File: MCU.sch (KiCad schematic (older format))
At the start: 14 parts, among them U1 STM32F405RGTx, U2 ADR4533BRZ, Y1 Crystal_GND24

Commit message: Finished first version of schematic
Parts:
- C20: renamed from C3; footprint (none) -> Capacitor_SMD:C_0603_1608Metric
- C21: renamed from C4; footprint (none) -> Capacitor_SMD:C_0603_1608Metric
- C22: renamed from C5; footprint (none) -> Capacitor_SMD:C_0603_1608Metric
- C23: renamed from C6; footprint (none) -> Capacitor_SMD:C_0603_1608Metric
- C24: renamed from C7; footprint (none) -> Capacitor_SMD:C_0603_1608Metric
- C25: renamed from C8; footprint (none) -> Capacitor_SMD:C_0603_1608Metric
- C26: renamed from C9; footprint (none) -> Capacitor_SMD:C_0603_1608Metric
- C27: renamed from C10; footprint (none) -> Capacitor_SMD:C_0603_1608Metric
- C28: renamed from C11; footprint (none) -> Capacitor_SMD:C_0603_1608Metric
- C29: renamed from C12; footprint (none) -> Capacitor_SMD:C_0603_1608Metric
- C30: renamed from C13; footprint (none) -> Capacitor_SMD:C_0603_1608Metric
- Y1: footprint (none) -> Crystal:Crystal_SMD_Abracon_ABM3C-4Pin_5.0x3.2mm
- renumbered U1 to U7, U2 to U8
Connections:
- net labels added: PB7_OUT_EN, PC2_ADC123_12, PC3_ADC123_13
- net labels removed: GNDA, PB7_VSEL_6, PB8_VSEL_7, PB9_VSEL_8
- no-connect marks 0 -> 18
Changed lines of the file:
@@
 $Descr A4 11693 8268
 encoding utf-8
-Sheet 2 4
-Title ""
-Date ""
-Rev ""
-Comp ""
+Sheet 4 5
+Title "Z Sim"
+Date "2019-10-22"
+Rev "0.1"
+Comp "ELp"
 Comment1 ""
 Comment2 ""
@@
 $EndDescr
 $Comp
-L MCU_ST_STM32F4:STM32F405RGTx U1
+L MCU_ST_STM32F4:STM32F405RGTx U7
 U 1 1 5DADBC00
 P 5750 3600
-F 0 "U1" H 5150 1811 50  0000 C CNN
+F 0 "U7" H 5150 1811 50  0000 C CNN
 F 1 "STM32F405RGTx" H 5150 1720 50  0000 C CNN
 F 2 "Package_QFP:LQFP-64_10x10mm_P0.5mm" H 5150 1900 50  0001 R CNN
@@
 	5050 3300 4450 3300
 $Comp
-L power:GND #PWR0111
+L power:GND #PWR031
 U 1 1 5DAEB085
 P 3050 3250
-F 0 "#PWR0111" H 3050 3000 50  0001 C CNN
+F 0 "#PWR031" H 3050 3000 50  0001 C CNN
 F 1 "GND" H 3055 3077 50  0000 C CNN
 F 2 "" H 3050 3250 50  0001 C CNN
@@
 $EndComp
 $Comp
-L Device:C_Small C8
+L Device:C_Small C25
 U 1 1 5DAEB516
 P 4750 2350
-F 0 "C8" V 4700 2450 50  0000 C CNN
+F 0 "C25" V 4700 2450 50  0000 C CNN
 F 1 "2.2u" V 4800 2500 50  0000 C CNN
-F 2 "" H 4750 2350 50  0001 C CNN
+F 2 "Capacitor_SMD:C_0603_1608Metric" H 4750 2350 50  0001 C CNN
 F 3 "~" H 4750 2350 50  0001 C CNN
 	1    4750 2350
@@
 $EndComp
 $Comp
-L Device:C_Small C9
+L Device:C_Small C26
 U 1 1 5DAECD7A
 P 4750 2550
-F 0 "C9" V 4700 2650 50  0000 C CNN
+F 0 "C26" V 4700 2650 50  0000 C CNN
 F 1 "2.2u" V 4800 2700 50  0000 C CNN
-F 2 "" H 4750 2550 50  0001 C CNN
+F 2 "Capacitor_SMD:C_0603_1608Metric" H 4750 2550 50  0001 C CNN
 F 3 "~" H 4750 2550 50  0001 C CNN
 	1    4750 2550
@@
 	3900 2700 3900 2950
 $Comp
-L Device:C_Small C3
+L Device:C_Small C20
 U 1 1 5DAE6AD0
 P 3350 2850
-F 0 "C3" H 3442 2896 50  0000 L CNN
+F 0 "C20" H 3442 2896 50  0000 L CNN
 F 1 "22p" H 3442 2805 50  0000 L CNN
-F 2 "" H 3350 2850 50  0001 C CNN
+F 2 "Capacitor_SMD:C_0603_1608Metric" H 3350 2850 50  0001 C CNN
 F 3 "~" H 3350 2850 50  0001 C CNN
 	1    3350 2850
@@
 $EndComp
 $Comp
-L Device:C_Small C4
+L Device:C_Small C21
 U 1 1 5DAE66B4
 P 3350 3450
-F 0 "C4" H 3442 3496 50  0000 L CNN
+F 0 "C21" H 3442 3496 50  0000 L CNN
 F 1 "22p" H 3442 3405 50  0000 L CNN
-F 2 "" H 3350 3450 50  0001 C CNN
+F 2 "Capacitor_SMD:C_0603_1608Metric" H 3350 3450 50  0001 C CNN
 F 3 "~" H 3350 3450 50  0001 C CNN
 	1    3350 3450
@@
 F 0 "Y1" V 3854 3494 50  0000 L CNN
 F 1 "Crystal_GND24" V 3550 3300 50  0000 L CNN
-F 2 "" H 3900 3250 50  0001 C CNN
+F 2 "Crystal:Crystal_SMD_Abracon_ABM3C-4Pin_5.0x3.2mm" H 3900 3250 50  0001 C CNN
 F 3 "~" H 3900 3250 50  0001 C CNN
 	1    3900 3250
@@
 	3350 3250 3700 3250
 $Comp
-L power:GND #PWR0112
+L power:GND #PWR034
 U 1 1 5DAF9103
 P 4600 2650
-F 0 "#PWR0112" H 4600 2400 50  0001 C CNN
+F 0 "#PWR034" H 4600 2400 50  0001 C CNN
 F 1 "GND" H 4750 2550 50  0000 C CNN
 F 2 "" H 4600 2650 50  0001 C CNN
@@
 	4450 3200 5050 3200
 $Comp
-L Device:C_Small C11
+L Device:C_Small C28
 U 1 1 5DB007EA
 P 5000 1400
-F 0 "C11" V 4950 1600 50  0000 C CNN
+F 0 "C28" V 4950 1600 50  0000 C CNN
 F 1 "2.2u" V 5050 1550 50  0000 C CNN
-F 2 "" H 5000 1400 50  0001 C CNN
+F 2 "Capacitor_SMD:C_0603_1608Metric" H 5000 1400 50  0001 C CNN
 F 3 "~" H 5000 1400 50  0001 C CNN
 	1    5000 1400
@@
 $EndComp
 $Comp
-L Device:C_Small C10
+L Device:C_Small C27
 U 1 1 5DB01DE1
 P 4800 1400
-F 0 "C10" V 4750 1600 50  0000 C CNN
+F 0 "C27" V 4750 1600 50  0000 C CNN
 F 1 "2.2u" V 4850 1550 50  0000 C CNN
-F 2 "" H 4800 1400 50  0001 C CNN
+F 2 "Capacitor_SMD:C_0603_1608Metric" H 4800 1400 50  0001 C CNN
 F 3 "~" H 4800 1400 50  0001 C CNN
 	1    4800 1400
@@
 $EndComp
 $Comp
-L Device:C_Small C7
+L Device:C_Small C24
 U 1 1 5DB0237F
 P 4600 1400
-F 0 "C7" V 4550 1600 50  0000 C CNN
+F 0 "C24" V 4550 1600 50  0000 C CNN
 F 1 "2.2u" V 4650 1550 50  0000 C CNN
-F 2 "" H 4600 1400 50  0001 C CNN
+F 2 "Capacitor_SMD:C_0603_1608Metric" H 4600 1400 50  0001 C CNN
 F 3 "~" H 4600 1400 50  0001 C CNN
 	1    4600 1400
@@
 $EndComp
 $Comp
-L Device:C_Small C6
+L Device:C_Small C23
 U 1 1 5DB0256C
 P 4400 1400
-F 0 "C6" V 4350 1600 50  0000 C CNN
+F 0 "C23" V 4350 1600 50  0000 C CNN
 F 1 "2.2u" V 4450 1550 50  0000 C CNN
-F 2 "" H 4400 1400 50  0001 C CNN
+F 2 "Capacitor_SMD:C_0603_1608Metric" H 4400 1400 50  0001 C CNN
 F 3 "~" H 4400 1400 50  0001 C CNN
 	1    4400 1400
@@
 $EndComp
 $Comp
-L Device:C_Small C5
+L Device:C_Small C22
 U 1 1 5DB027C5
 P 4200 1400
-F 0 "C5" V 4150 1600 50  0000 C CNN
+F 0 "C22" V 4150 1600 50  0000 C CNN
 F 1 "2.2u" V 4250 1550 50  0000 C CNN
-F 2 "" H 4200 1400 50  0001 C CNN
+F 2 "Capacitor_SMD:C_0603_1608Metric" H 4200 1400 50  0001 C CNN
 F 3 "~" H 4200 1400 50  0001 C CNN
 	1    4200 1400
@@
 $EndComp
 $Comp
-L power:GND #PWR0113
+L power:GND #PWR033
 U 1 1 5DB02CA7
 P 4200 1750
-F 0 "#PWR0113" H 4200 1500 50  0001 C CNN
+F 0 "#PWR033" H 4200 1500 50  0001 C CNN
 F 1 "GND" H 4205 1577 50  0000 C CNN
 F 2 "" H 4200 1750 50  0001 C CNN
@@
 	5550 1200 5650 1200
 $Comp
-L power:+3.3V #PWR0114
+L power:+3.3V #PWR032
 U 1 1 5DB07A5A
 P 4200 1100
-F 0 "#PWR0114" H 4200 950 50  0001 C CNN
+F 0 "#PWR032" H 4200 950 50  0001 C CNN
 F 1 "+3.3V" H 4215 1273 50  0000 C CNN
 F 2 "" H 4200 1100 50  0001 C CNN
@@
 Connection ~ 4200 1200
 $Comp
-L power:GND #PWR0115
+L power:GND #PWR035
 U 1 1 5DB08336
 P 5650 5650
-F 0 "#PWR0115" H 5650 5400 50  0001 C CNN
+F 0 "#PWR035" H 5650 5400 50  0001 C CNN
 F 1 "GND" H 5655 5477 50  0000 C CNN
 F 2 "" H 5650 5650 50  0001 C CNN
@@
 Wire Wire Line
 	5650 5550 5650 5650
-$Comp
-L power:GNDA #PWR0116
-U 1 1 5DB0BC7C
-P 5850 5650
-F 0 "#PWR0116" H 5850 5400 50  0001 C CNN
-F 1 "GNDA" H 5855 5477 50  0000 C CNN
-F 2 "" H 5850 5650 50  0001 C CNN
-F 3 "" H 5850 5650 50  0001 C CNN
-	1    5850 5650
-	1    0    0    -1
-$EndComp
 Wire Wire Line
 	5850 5650 5850 5400
@@
 Connection ~ 6750 1600
 $Comp
-L Device:C_Small C12
+L Device:C_Small C29
 U 1 1 5DAFDB37
 P 6750 1350
-F 0 "C12" V 6700 1500 50  0000 C CNN
+F 0 "C29" V 6700 1500 50  0000 C CNN
 F 1 "2.2u" V 6800 1500 50  0000 C CNN
-F 2 "" H 6750 1350 50  0001 C CNN
+F 2 "Capacitor_SMD:C_0603_1608Metric" H 6750 1350 50  0001 C CNN
 F 3 "~" H 6750 1350 50  0001 C CNN
 	1    6750 1350
@@
 	6750 1600 6750 1700
 $Comp
-L power:+5V #PWR0117
+L power:+5V #PWR039
 U 1 1 5DB117FC
 P 7350 1000
-F 0 "#PWR0117" H 7350 850 50  0001 C CNN
+F 0 "#PWR039" H 7350 850 50  0001 C CNN
 F 1 "+5V" H 7365 1173 50  0000 C CNN
 F 2 "" H 7350 1000 50  0001 C CNN
@@
 $EndComp
 $Comp
-L power:+3.3VA #PWR0118
+L power:+3.3VA #PWR037
 U 1 1 5DB122D6
 P 6750 1000
-F 0 "#PWR0118" H 6750 850 50  0001 C CNN
+F 0 "#PWR037" H 6750 850 50  0001 C CNN
 F 1 "+3.3VA" H 6765 1173 50  0000 C CNN
 F 2 "" H 6750 1000 50  0001 C CNN
@@
 	7600 1600 7350 1600
 $Comp
-L rise_elp:ADR4533BRZ U2
+L rise_elp:ADR4533BRZ U8
 U 1 1 5DB0F4BD
 P 7950 1400
-F 0 "U2" H 7950 1865 50  0000 C CNN
+F 0 "U8" H 7950 1865 50  0000 C CNN
 F 1 "ADR4533BRZ" H 7950 1774 50  0000 C CNN
 F 2 "Package_SO:SOIC-8_3.9x4.9mm_P1.27mm" H 7950 1400 50  0001 C CNN
@@
 $EndComp
 $Comp
-L Device:C_Small C13
+L Device:C_Small C30
 U 1 1 5DB10D58
 P 7350 1450
-F 0 "C13" V 7200 1450 50  0000 C CNN
+F 0 "C30" V 7200 1450 50  0000 C CNN
 F 1 "2.2u" V 7450 1450 50  0000 C CNN
-F 2 "" H 7350 1450 50  0001 C CNN
+F 2 "Capacitor_SMD:C_0603_1608Metric" H 7350 1450 50  0001 C CNN
 F 3 "~" H 7350 1450 50  0001 C CNN
 	1    7350 1450
 	-1   0    0    1
-$EndComp
-$Comp
-L power:GNDA #PWR0119
-U 1 1 5DB0C478
-P 6750 1700
-F 0 "#PWR0119" H 6750 1450 50  0001 C CNN
-F 1 "GNDA" H 6755 1527 50  0000 C CNN
-F 2 "" H 6750 1700 50  0001 C CNN
-F 3 "" H 6750 1700 50  0001 C CNN
-	1    6750 1700
-	1    0    0    -1
 $EndComp
 Wire Wire Line
@@
 Text HLabel 6450 4200 2    50   Input ~ 0
 PB5_VSEL_4
-Text HLabel 6450 4600 2    50   Input ~ 0
-PB9_VSEL_8
-Text HLabel 6450 4500 2    50   Input ~ 0
-PB8_VSEL_7
-Text HLabel 6450 4400 2    50   Input ~ 0
-PB7_VSEL_6
 Text HLabel 6450 4300 2    50   Input ~ 0
 PB6_VSEL_5
@@
 Text HLabel 5050 5000 0    50   Input ~ 0
 SDIO_DET
+Text HLabel 6450 4400 2    50   Input ~ 0
+PB7_OUT_EN
+Text HLabel 5050 3900 0    50   Input ~ 0
+PC2_ADC123_12
+Text HLabel 5050 4000 0    50   Input ~ 0
+PC3_ADC123_13
+NoConn ~ 5050 4100
+NoConn ~ 5050 4200
+NoConn ~ 5050 4300
+NoConn ~ 5050 4400
+NoConn ~ 5050 5100
+NoConn ~ 5050 5200
+NoConn ~ 6450 5200
+NoConn ~ 6450 5100
+NoConn ~ 6450 5000
+NoConn ~ 6450 4900
+NoConn ~ 6450 4800
+NoConn ~ 6450 4700
+NoConn ~ 6450 4600
+NoConn ~ 6450 4500
+NoConn ~ 6450 3500
+NoConn ~ 6450 3000
+NoConn ~ 6450 2900
+NoConn ~ 6450 2800
+$Comp
+L power:GND #PWR0105
+U 1 1 5DB6234C
+P 5850 5650
+F 0 "#PWR0105" H 5850 5400 50  0001 C CNN
+F 1 "GND" H 5855 5477 50  0000 C CNN
+F 2 "" H 5850 5650 50  0001 C CNN
+F 3 "" H 5850 5650 50  0001 C CNN
+	1    5850 5650
+	1    0    0    -1
+$EndComp
+$Comp
+L power:GND #PWR0106
+U 1 1 5DB5AF69
+P 6750 1700
+F 0 "#PWR0106" H 6750 1450 50  0001 C CNN
+F 1 "GND" H 6755 1527 50  0000 C CNN
+F 2 "" H 6750 1700 50  0001 C CNN
+F 3 "" H 6750 1700 50  0001 C CNN
+	1    6750 1700
+	1    0    0    -1
+$EndComp
 $EndSCHEMATC

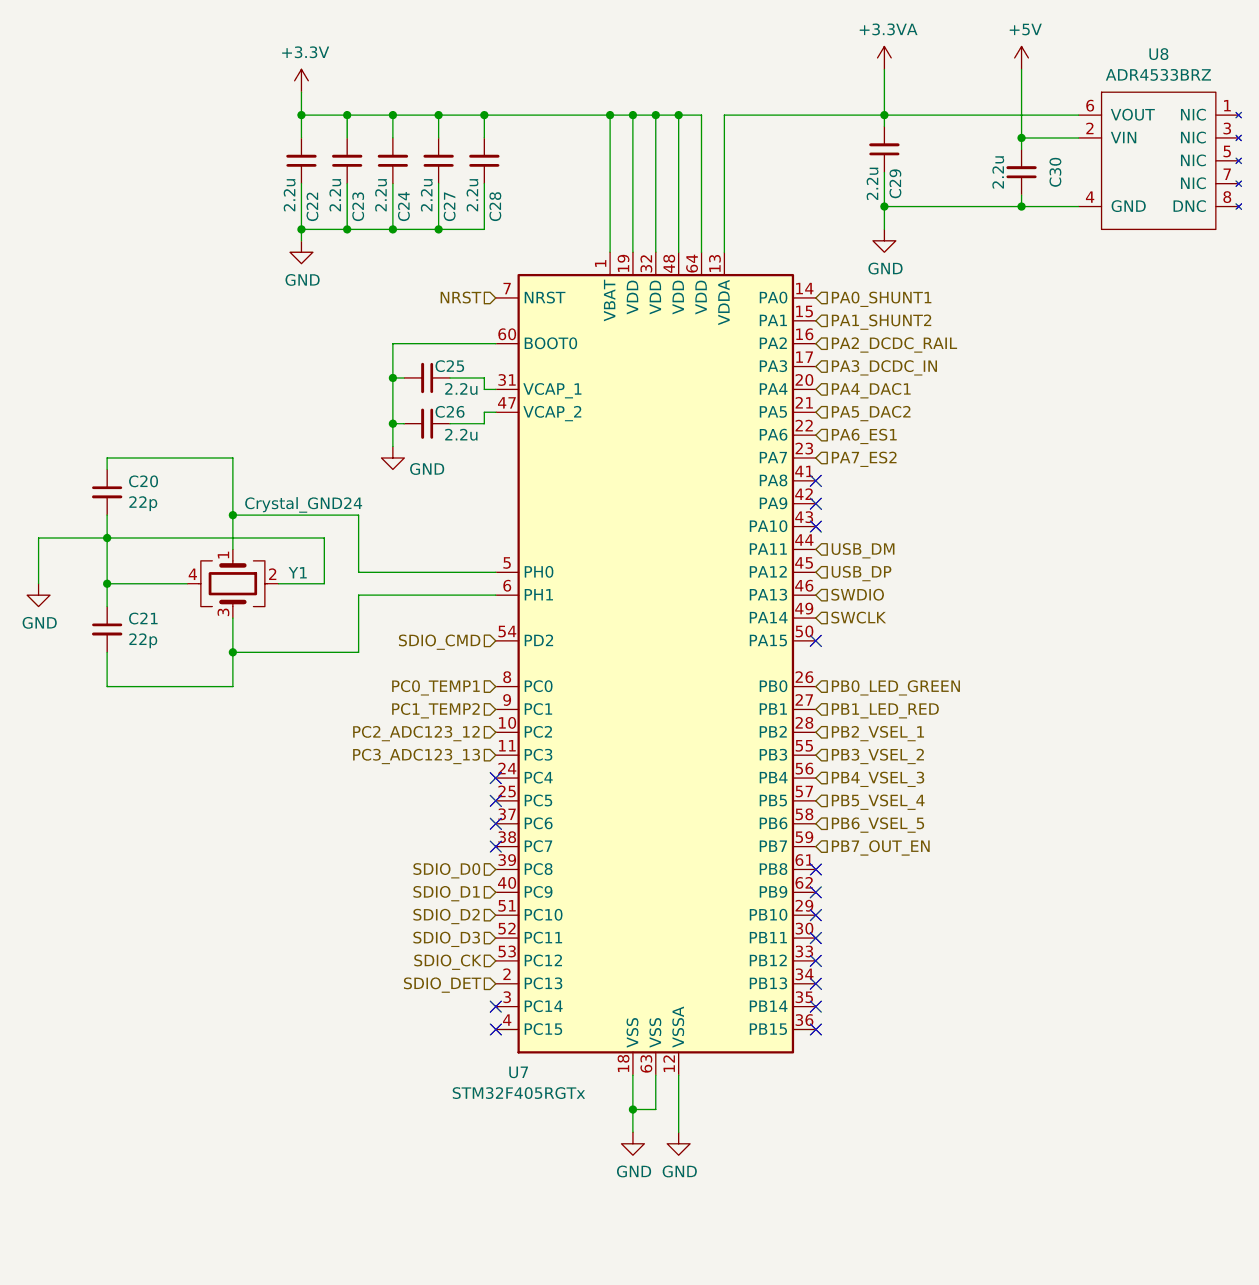
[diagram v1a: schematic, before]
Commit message: Schematic updates, added 3D models and started routing
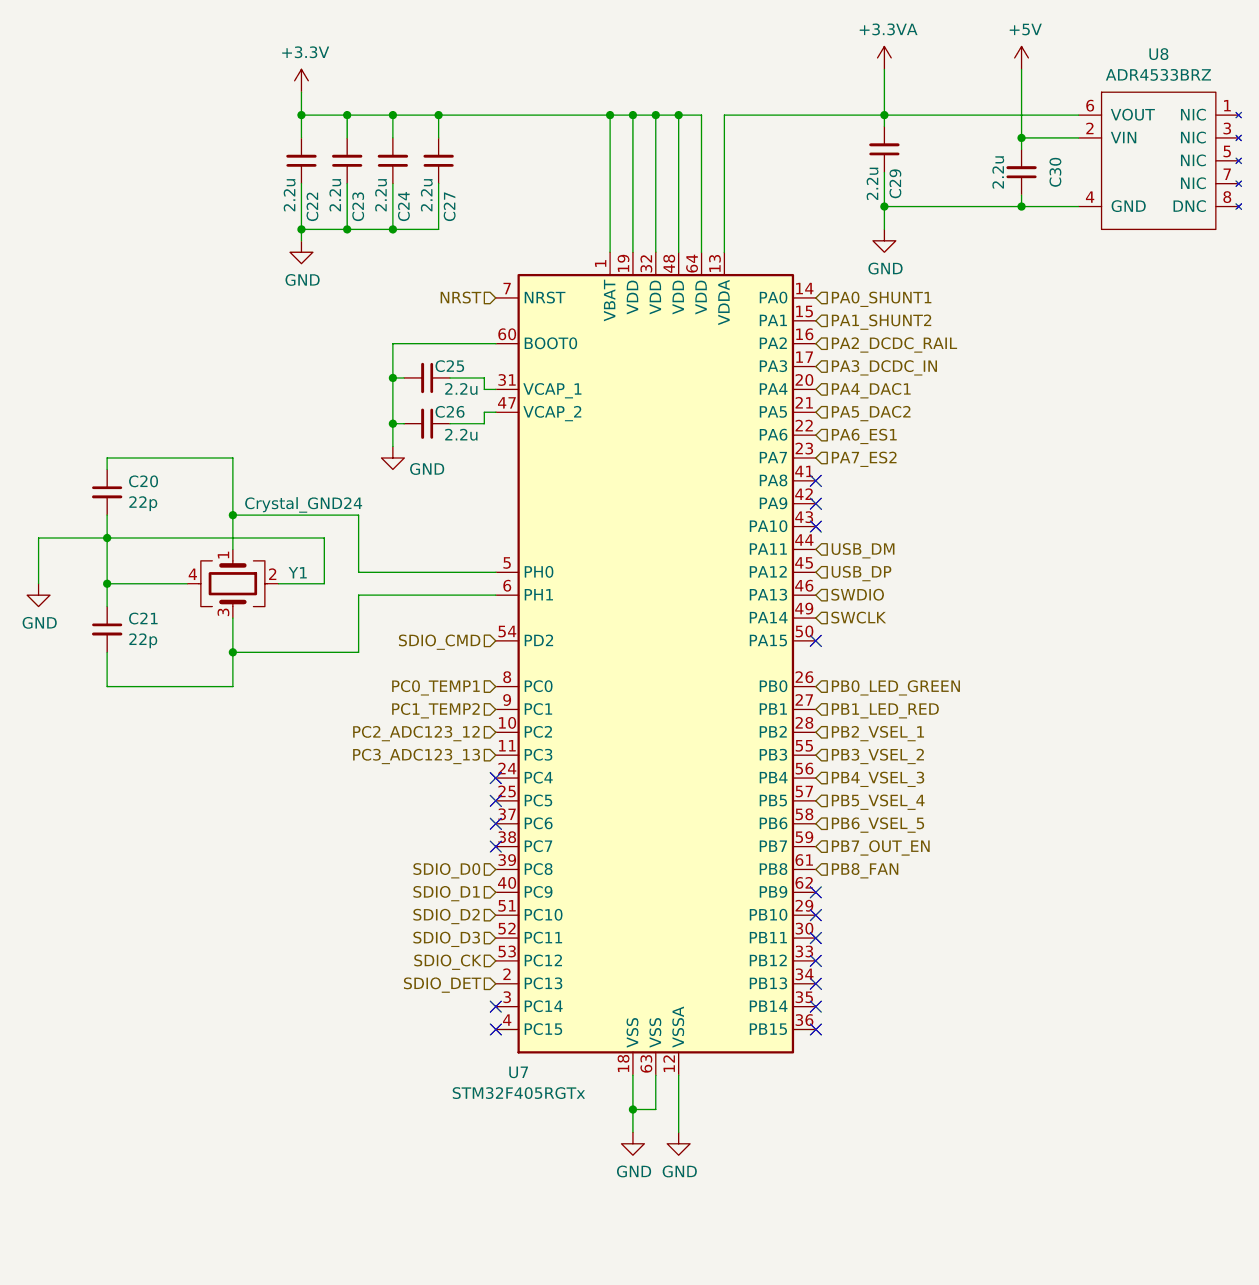
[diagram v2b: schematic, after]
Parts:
- removed C28: 2.2u, Capacitor_SMD:C_0603_1608Metric, symbol Device:C_Small
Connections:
- net PB8_FAN: now reaches U7.61 (PB8)
- no-connect marks 18 -> 17
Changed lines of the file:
@@
 	4450 3200 5050 3200
-$Comp
-L Device:C_Small C28
-U 1 1 5DB007EA
-P 5000 1400
-F 0 "C28" V 4950 1600 50  0000 C CNN
-F 1 "2.2u" V 5050 1550 50  0000 C CNN
-F 2 "Capacitor_SMD:C_0603_1608Metric" H 5000 1400 50  0001 C CNN
-F 3 "~" H 5000 1400 50  0001 C CNN
-	1    5000 1400
-	-1   0    0    1
-$EndComp
 $Comp
 L Device:C_Small C27
@@
 Wire Wire Line
 	4200 1700 4400 1700
-Wire Wire Line
-	5000 1700 5000 1500
 Connection ~ 4200 1700
 Wire Wire Line
@@
 Wire Wire Line
 	4800 1500 4800 1700
-Connection ~ 4800 1700
-Wire Wire Line
-	4800 1700 5000 1700
 Wire Wire Line
 	4600 1500 4600 1700
@@
 	4800 1200 4600 1200
 Wire Wire Line
-	5000 1300 5000 1200
-Connection ~ 5000 1200
-Wire Wire Line
-	5000 1200 4800 1200
-Wire Wire Line
 	5850 1800 5850 1200
 Connection ~ 5850 1200
 Wire Wire Line
 	5750 1800 5750 1200
-Wire Wire Line
-	5000 1200 5550 1200
 Connection ~ 5750 1200
 Wire Wire Line
@@
 NoConn ~ 6450 4700
 NoConn ~ 6450 4600
-NoConn ~ 6450 4500
 NoConn ~ 6450 3500
 NoConn ~ 6450 3000
@@
 	1    0    0    -1
 $EndComp
+Wire Wire Line
+	4800 1200 5550 1200
+Text HLabel 6450 4500 2    50   Input ~ 0
+PB8_FAN
 $EndSCHEMATC

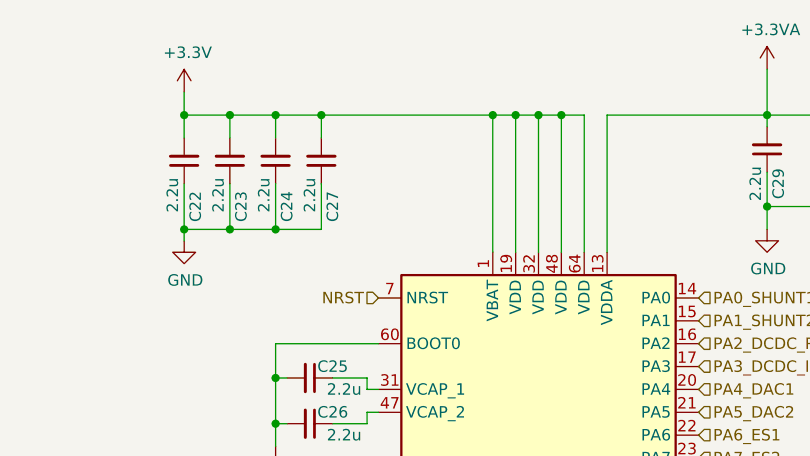
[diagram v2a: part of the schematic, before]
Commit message: Finished routing and added some 3D models
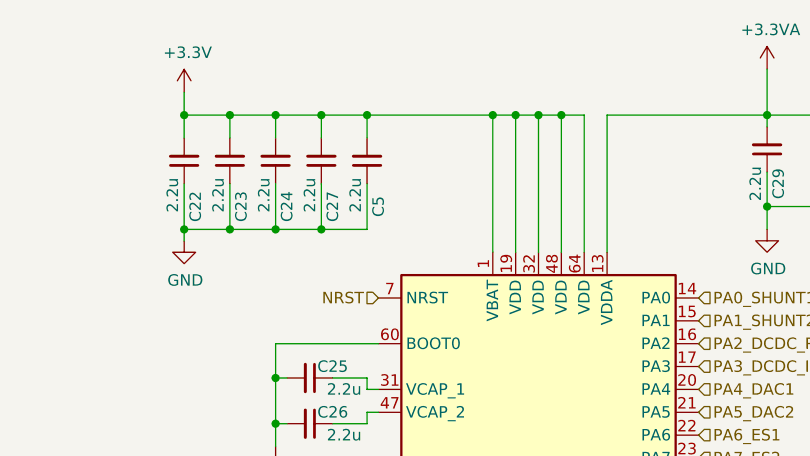
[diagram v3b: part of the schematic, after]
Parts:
- added C5: 2.2u, Capacitor_SMD:C_0603_1608Metric, symbol Device:C_Small
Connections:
- net +3V3: now also C5.2
- net GND: now also C5.1
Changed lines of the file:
@@
 $EndComp
 Wire Wire Line
-	4800 1200 5550 1200
+	4800 1200 5000 1200
 Text HLabel 6450 4500 2    50   Input ~ 0
 PB8_FAN
+$Comp
+L Device:C_Small C5
+U 1 1 5DBFF881
+P 5000 1400
+F 0 "C5" V 4950 1600 50  0000 C CNN
+F 1 "2.2u" V 5050 1550 50  0000 C CNN
+F 2 "Capacitor_SMD:C_0603_1608Metric" H 5000 1400 50  0001 C CNN
+F 3 "~" H 5000 1400 50  0001 C CNN
+	1    5000 1400
+	-1   0    0    1
+$EndComp
+Wire Wire Line
+	5000 1300 5000 1200
+Connection ~ 5000 1200
+Wire Wire Line
+	5000 1200 5550 1200
+Wire Wire Line
+	5000 1500 5000 1700
+Wire Wire Line
+	5000 1700 4800 1700
+Connection ~ 4800 1700
 $EndSCHEMATC
